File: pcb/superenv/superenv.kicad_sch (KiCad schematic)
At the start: 25 parts, among them J1 TYPE-C-31-M-04, J2 Power-Header, J3 UART, J4 I2C, J5 I2C, U1 ESP32-C6-WROOM-1, U2 AMS1117-3.3, U3 DS18B20, U4 DS18B20, U5 DS18B20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

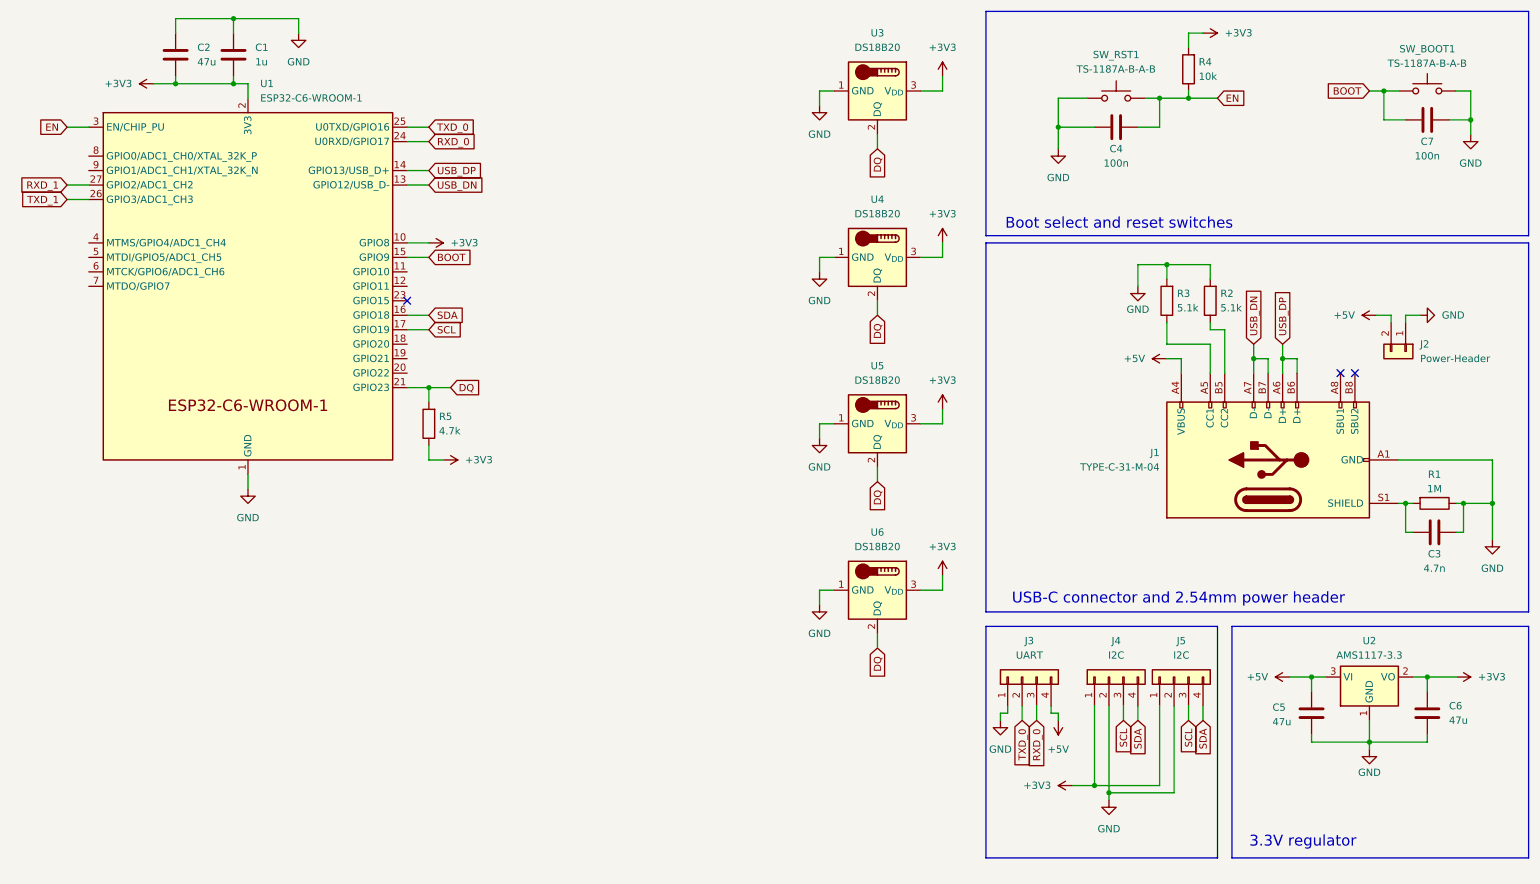
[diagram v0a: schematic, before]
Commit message: Add I2C pull ups
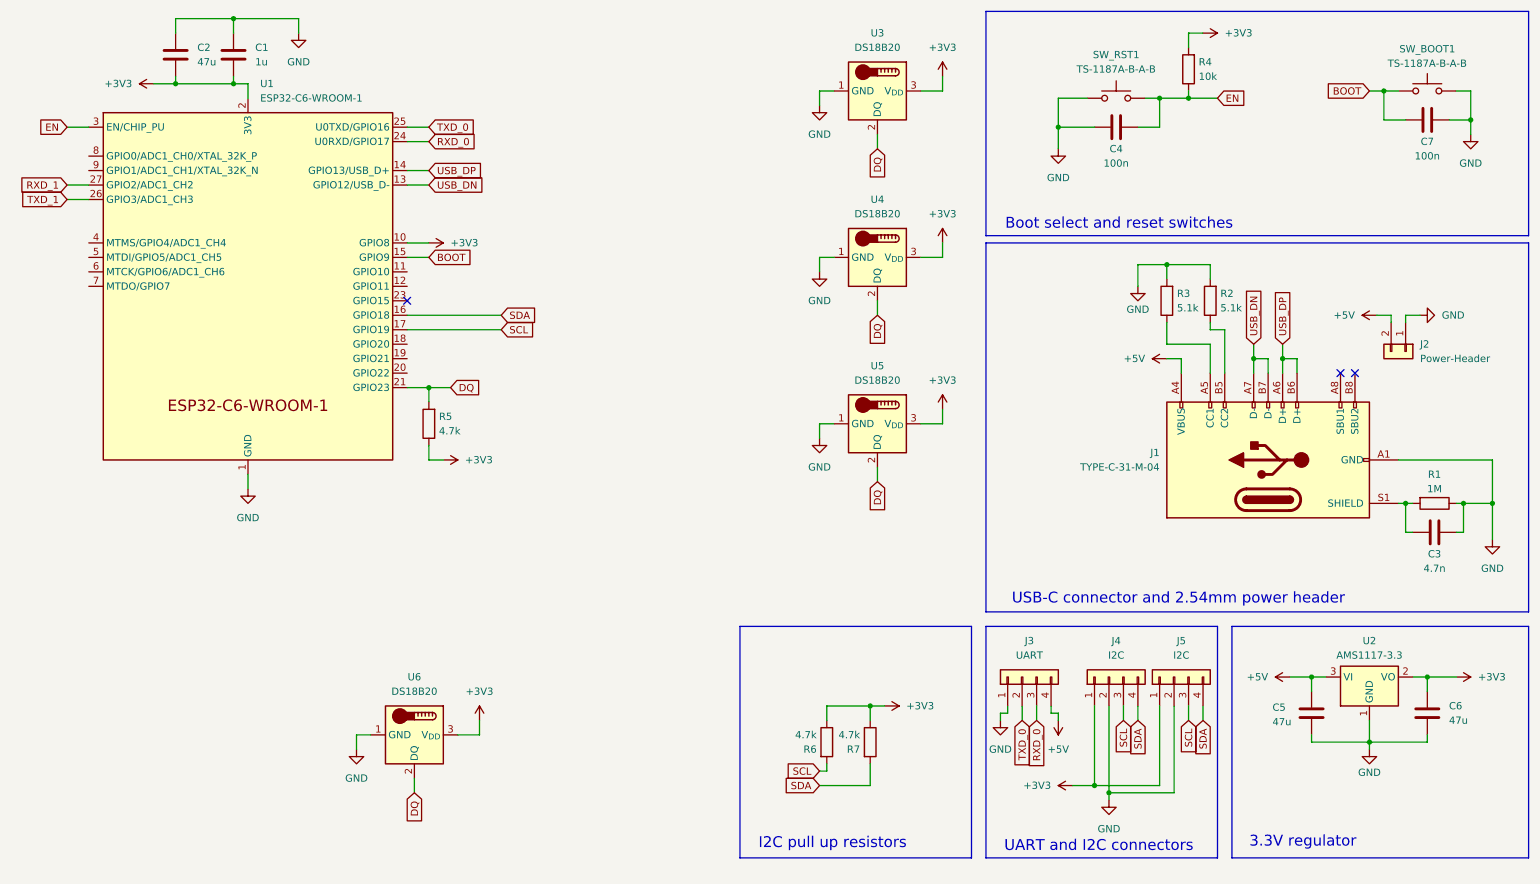
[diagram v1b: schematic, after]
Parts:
- added R6, R7: 4.7k, Resistor_SMD:R_0402_1005Metric, symbol Device:R
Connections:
- net +3V3: now also R6.1, R7.1
- net SCL: now also R6.2
- net SDA: now also R7.2
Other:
- note added: "I2C pull up resistors"
- note added: "UART and I2C connectors"
- moved on the sheet: U6

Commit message: Add I2C sensors
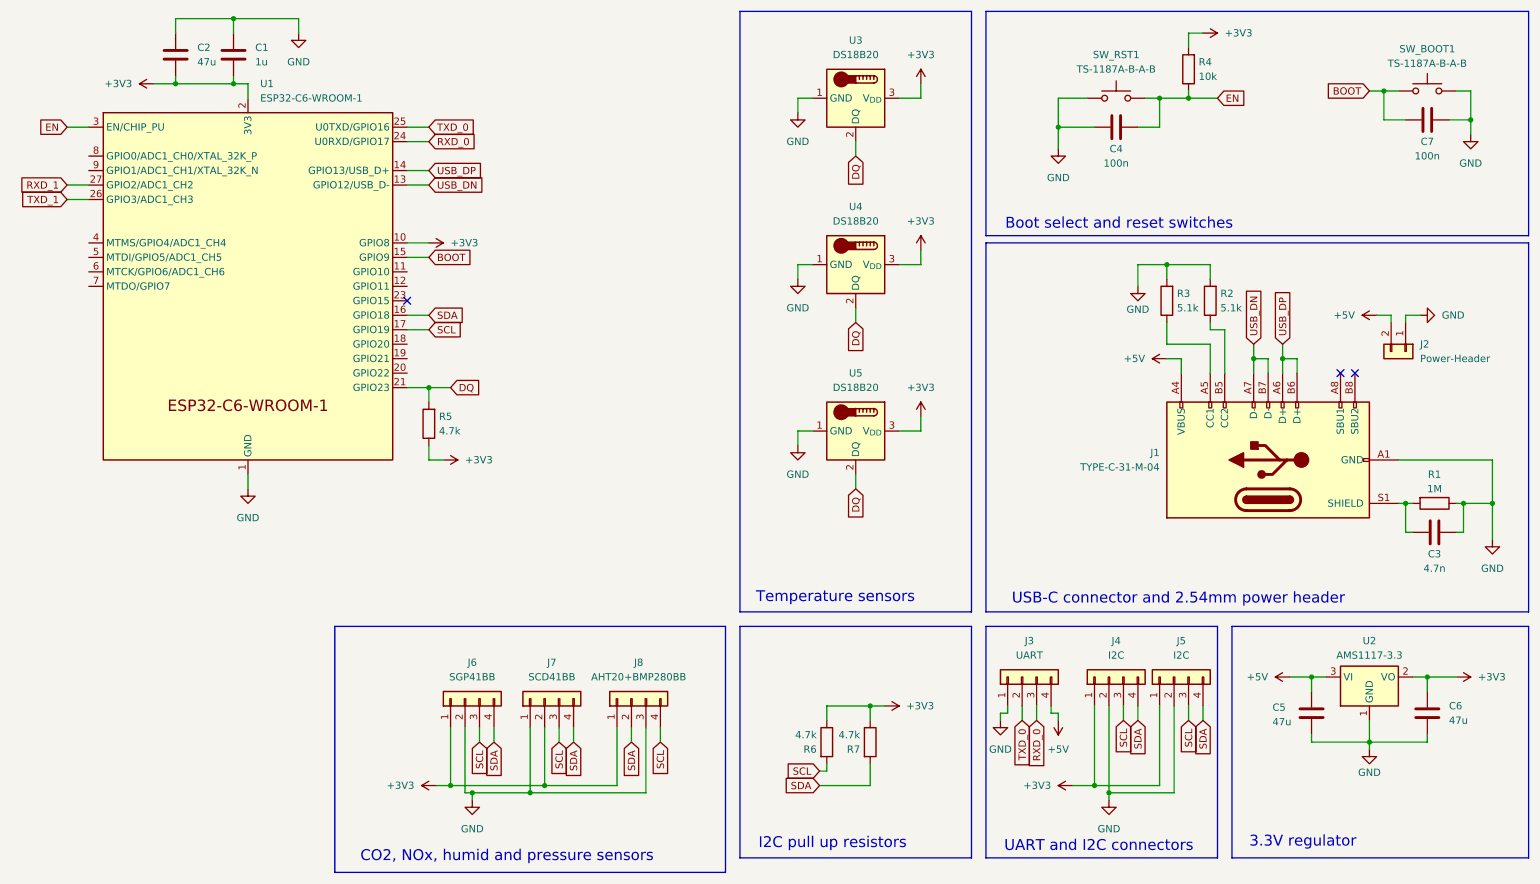
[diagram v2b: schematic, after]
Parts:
- removed U6: DS18B20, Package_TO_SOT_THT:TO-92_Inline, symbol Sensor_Temperature:DS18B20
- added J6: SGP41BB, Connector_PinHeader_2.54mm:PinHeader_1x04_P2.54mm_Vertical, symbol Connector_Generic:Conn_01x04
- added J7: SCD41BB, Connector_PinHeader_2.54mm:PinHeader_1x04_P2.54mm_Vertical, symbol Connector_Generic:Conn_01x04
- added J8: AHT20+BMP280BB, Connector_PinHeader_2.54mm:PinHeader_1x04_P2.54mm_Vertical, symbol Connector_Generic:Conn_01x04
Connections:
- net +3V3: now also J6.1 (Pin_1), J7.2 (Pin_2), J8.1 (Pin_1)
- net GND: now also J6.2 (Pin_2), J7.1 (Pin_1), J8.3 (Pin_3)
- net SCL: now also J6.3 (Pin_3), J7.3 (Pin_3), J8.4 (Pin_4)
- net SDA: now also J6.4 (Pin_4), J7.4 (Pin_4), J8.2 (Pin_2)
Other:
- note added: "CO2, NOx, humid and pressure sensors"
- note added: "Temperature sensors"
- moved on the sheet: U3, U4, U5

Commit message: Add stuff
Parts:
- added J10: PMSBB, Connector_JST:JST_GH_BM08B-GHS-TBT_1x08-1MP_P1.25mm_Vertical, symbol Connector_Generic:Conn_01x08
- added J9: UART1, Connector_PinHeader_2.54mm:PinHeader_1x04_P2.54mm_Vertical, symbol Connector_Generic:Conn_01x04
- J3: value UART -> UART0
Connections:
- net +5V: now also J9.4 (Pin_4)
- net GND: now also J9.1 (Pin_1)
- net RXD_1: now also J9.3 (Pin_3)
- net TXD_1: now also J9.2 (Pin_2)
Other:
- moved on the sheet: J3, J4, J5, J6, J7, J8, R6, R7
